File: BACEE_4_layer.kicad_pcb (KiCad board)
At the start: 2 copper layers, 41.1 x 24.8 mm, 17 parts, among them J1 Serial Port, J2 Digital pins, J3 I2C, J4 ISCP, U1 24LC1025, U2 DS1337S+, U3 24LC1025, U4 ATMEGA328-AU, Y1 Crystal 32KHz, Y2 Crystal 16MHz

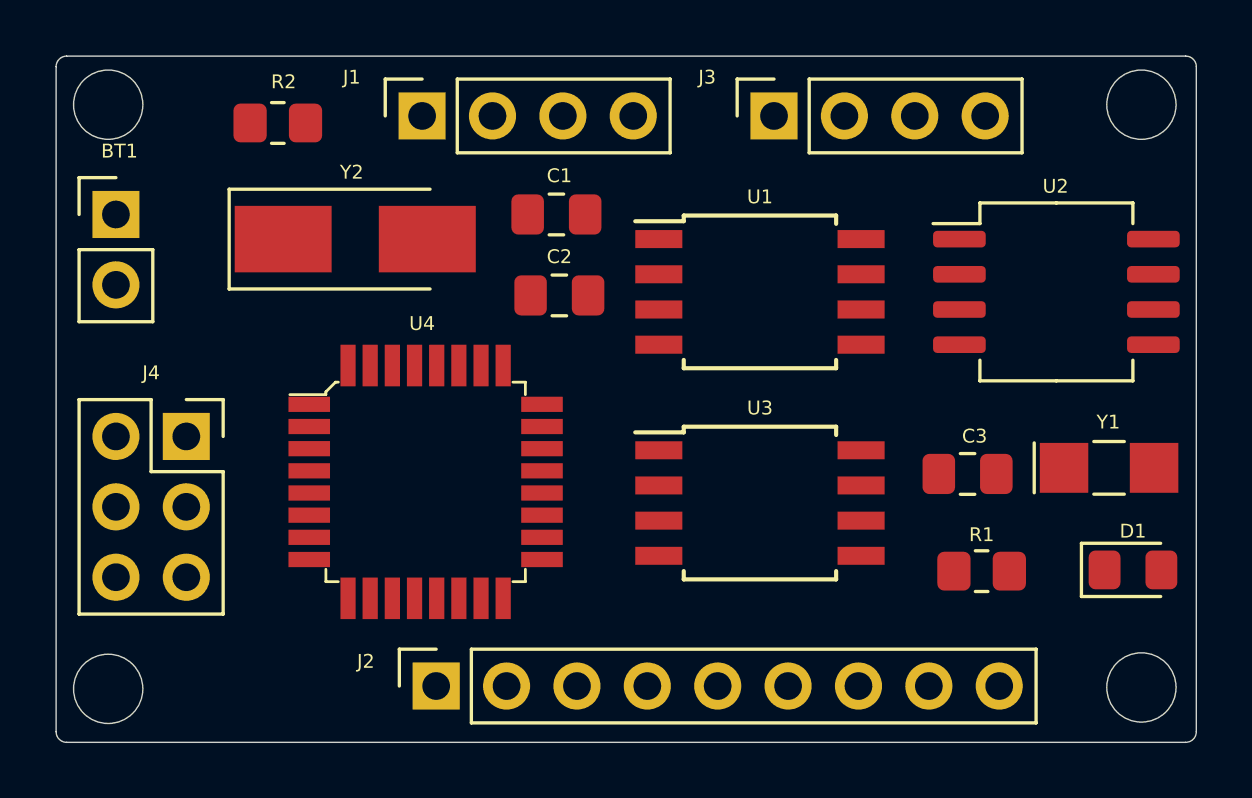
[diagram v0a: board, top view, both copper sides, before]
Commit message: Created copper filled area for board routed in 2 layers.
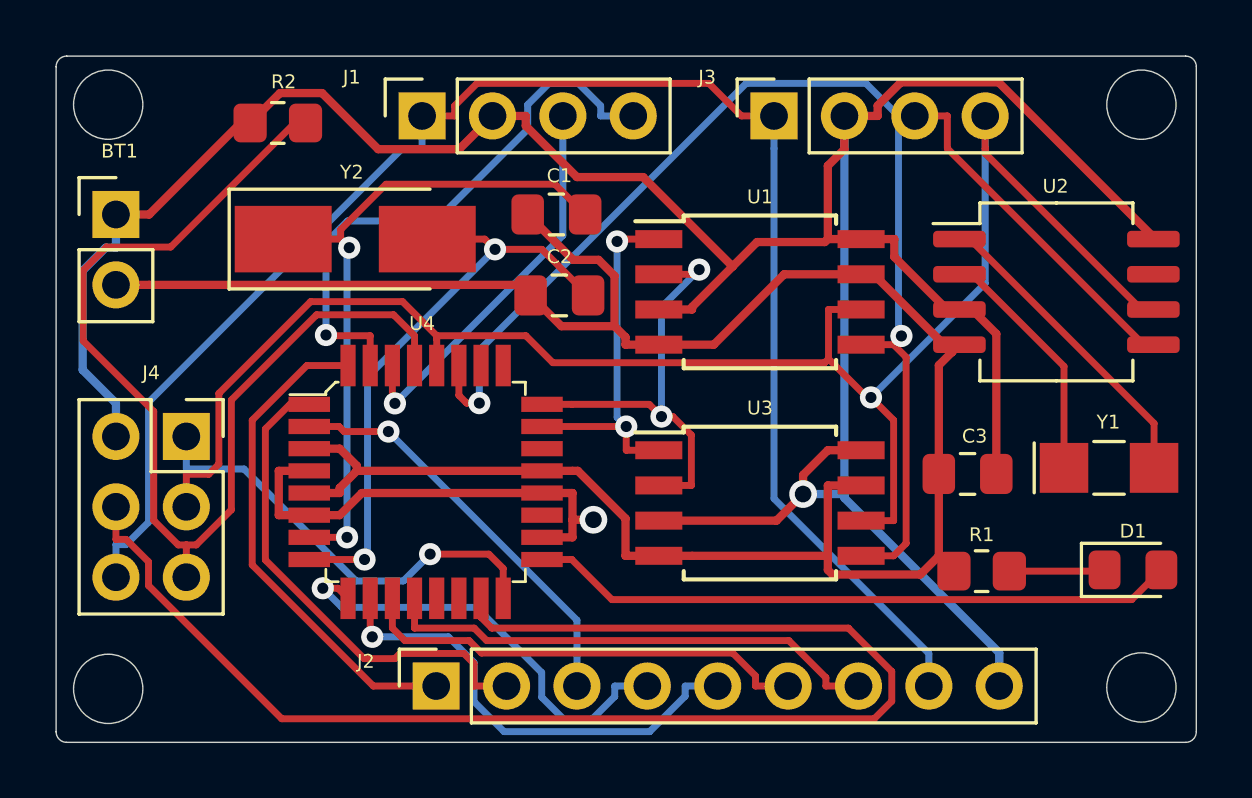
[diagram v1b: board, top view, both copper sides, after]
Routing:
- net /Vcc: track 0.00 -> 134.3 mm, vias 0 -> 2
- net GNDPWR: track 0.00 -> 80.0 mm
- net /SCL: track 0.00 -> 63.1 mm, vias 0 -> 1
- net /Connectors/GND: track 0.00 -> 58.6 mm
- net /SDA: track 0.00 -> 55.5 mm, vias 0 -> 2
- net /MOSI: track 0.00 -> 50.0 mm
- net /RESET: track 0.00 -> 38.4 mm
- net Net-(C1-Pad2): track 0.00 -> 24.7 mm, vias 0 -> 2
- net Net-(D1-Pad2): track 0.00 -> 23.4 mm
- net Net-(C2-Pad2): track 0.00 -> 21.8 mm, vias 0 -> 2
- net /TX: track 0.00 -> 20.7 mm, vias 0 -> 1
- net /D8: track 0.00 -> 18.1 mm
- net /D2: track 0.00 -> 17.9 mm
- net /D3: track 0.00 -> 17.9 mm
- net /D6: track 0.00 -> 17.0 mm, vias 0 -> 1
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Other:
- copper layers 2 -> 4
